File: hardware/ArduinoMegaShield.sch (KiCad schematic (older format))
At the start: 48 parts, among them P1 CONN_01X02, P10 CONN_01X02, P11 CONN_01X02, P12 CONN_01X02, P13 CONN_01X02, P14 CONN_01X02, P15 CONN_01X02, P16 CONN_01X02, P17 CONN_01X02, P18 CONN_01X02, P19 CONN_01X02, P2 CONN_01X02, P20 CONN_01X02, P21 CONN_01X02, P22 CONN_01X02, P3 CONN_01X02, P4 CONN_01X02, P5 CONN_01X02, P6 CONN_01X02, P7 CONN_01X02, P8 CONN_01X02, P9 CONN_01X02, U1 A4988, U2 A4988, U3 A4988

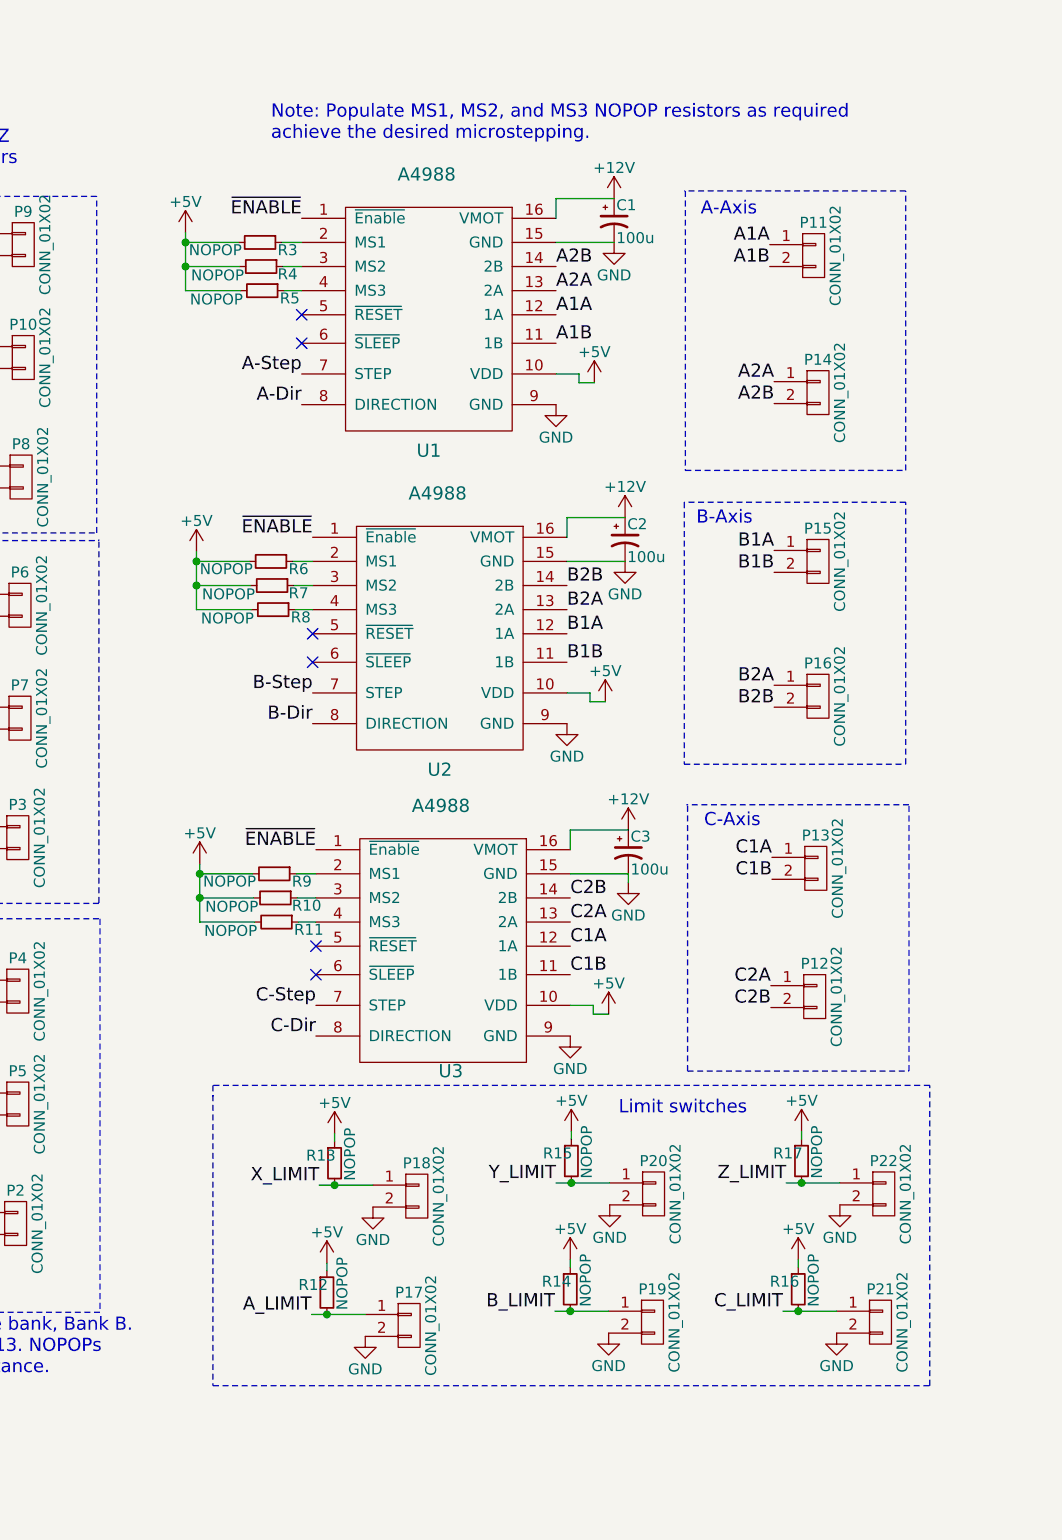
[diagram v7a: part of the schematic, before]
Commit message: added caps to the limit switches
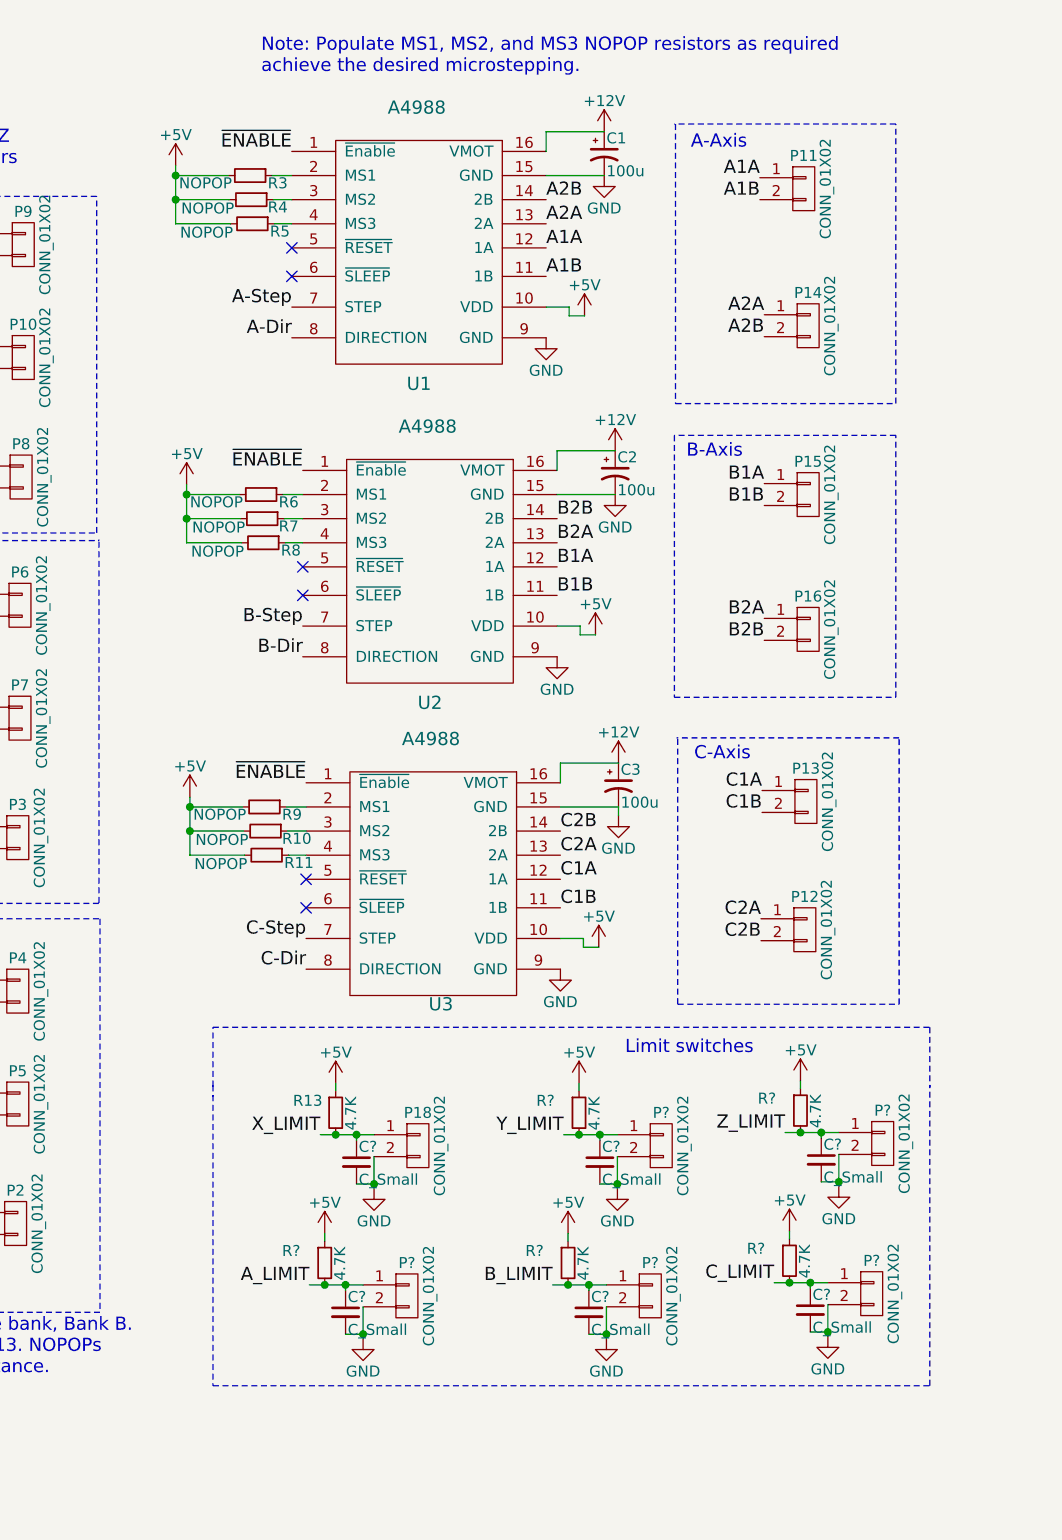
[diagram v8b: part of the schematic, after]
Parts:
- removed P17, P19, P20, P21, P22: CONN_01X02, 6axis:Terminal_Block_200_mil, symbol CONN_01X02
- removed R12, R14, R15, R16, R17: NOPOP, Resistors_SMD:R_0805_HandSoldering, symbol R_Small
- added C? (x6): C_Small, symbol C_Small
- added P? (x5): CONN_01X02, 6axis:Terminal_Block_200_mil, symbol CONN_01X02
- added R? (x5): 4.7K, Resistors_SMD:R_0805_HandSoldering, symbol R_Small
- R13: value NOPOP -> 4.7K; Fieldname (none) -> Value
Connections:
- net +5V: now also R?.1, R?.1, R?.1, R?.1, R?.1
- net A_LIMIT: now also C?.1, P?.1 (P1), R?.2
- net B_LIMIT: now also C?.1, P?.1 (P1), R?.2
- net C_LIMIT: now also C?.1, P?.1 (P1), R?.2
- net GND: now also C?.2, C?.2, C?.2, C?.2, C?.2, C?.2, P?.2 (P2), P?.2 (P2), P?.2 (P2), P?.2 (P2), P?.2 (P2)
- net X_LIMIT: now also C?.1
- net Y_LIMIT: now also C?.1, P?.1 (P1), R?.2
- net Z_LIMIT: now also C?.1, P?.1 (P1), R?.2
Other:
- moved on the sheet: C1, C2, C3, P11, P12, P13, P14, P15, P16, P18, R10, R11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
